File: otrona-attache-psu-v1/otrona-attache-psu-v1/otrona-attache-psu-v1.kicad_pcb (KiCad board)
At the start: 2 copper layers, 258 x 103 mm, 0 parts

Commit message: [otrona] Update schematic, layout, part selection
so far so good... now to print it out and see
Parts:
- added C1: 100uF, Capacitor_THT:CP_Radial_D10.0mm_P5.00mm, F.Cu at (213.9, 44.7)
- added C2: 100uF, Capacitor_THT:CP_Radial_D10.0mm_P5.00mm, F.Cu at (214.1, 26.7)
- added C3: 100uF, Capacitor_THT:CP_Radial_D10.0mm_P5.00mm, F.Cu at (233.2, 84.8)
- added C4: 100uF, Capacitor_THT:CP_Radial_D10.0mm_P5.00mm, F.Cu at (214.1, 14.0)
- added J1: VIDEO, Connector_Phoenix_MSTB:PhoenixContact_MSTBVA_2,5_5-G-5,08_1x05_P5.08mm_Vertical, F.Cu at (250.6, 95.0)
- added J2: CPU, Connector_Phoenix_MSTB:PhoenixContact_MSTBVA_2,5_12-G-5,08_1x12_P5.08mm_Vertical, F.Cu at (232.8, 66.7)
- added J3: DRIVES, Connector_Phoenix_MSTB:PhoenixContact_MSTBVA_2,5_8-G-5,08_1x08_P5.08mm_Vertical, F.Cu at (250.6, 46.1)
- added J4: 15V_CONV, Connector_PinHeader_2.54mm:PinHeader_1x04_P2.54mm_Horizontal, F.Cu at (210.5, 96.6)
- added J5: ATX-24, Connector_Molex:Molex_Mini-Fit_Jr_5566-24A2_2x12_P4.20mm_Vertical, F.Cu at (166.7, 60.9)
- added J6: PWR, Connector_PinHeader_2.54mm:PinHeader_1x02_P2.54mm_Horizontal, F.Cu at (171.5, 94.3)
- added J7: FAN, Connector_PinHeader_2.54mm:PinHeader_1x02_P2.54mm_Horizontal, F.Cu at (162.7, 94.3)
- added L1: 100uH, Inductor_THT:L_Axial_L11.0mm_D4.5mm_P15.24mm_Horizontal_Fastron_MECC, F.Cu at (222.9, 77.4)
- added L2: 100uH, Inductor_THT:L_Axial_L11.0mm_D4.5mm_P15.24mm_Horizontal_Fastron_MECC, F.Cu at (202.3, 34.0)
- added L3: 100uH, Inductor_THT:L_Axial_L11.0mm_D4.5mm_P15.24mm_Horizontal_Fastron_MECC, F.Cu at (202.3, 21.2)
- added L4: 100uH, Inductor_THT:L_Axial_L11.0mm_D4.5mm_P15.24mm_Horizontal_Fastron_MECC, F.Cu at (202.1, 10.1)
- added L5: 100uH, Inductor_THT:L_Axial_L11.0mm_D4.5mm_P15.24mm_Horizontal_Fastron_MECC, F.Cu at (223.0, 60.3)
- added L6: 100uH, Inductor_THT:L_Axial_L11.0mm_D4.5mm_P15.24mm_Horizontal_Fastron_MECC, F.Cu at (186.6, 77.3)

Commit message: [otrona] ok fine i routed the damned board
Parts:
- added J8: AUDIO, Connector_PinHeader_2.54mm:PinHeader_1x02_P2.54mm_Horizontal, F.Cu at (73.0, 109.2)
- moved L2 157.4 mm to (47.6, 63.0), turned to 270 degrees
- moved L3 156.2 mm to (47.6, 42.1), turned to 270 degrees
- moved J3 155.1 mm to (96.6, 64.8)
- moved L4 155.0 mm to (47.6, 21.3), turned to 270 degrees
- moved C3 154.1 mm to (79.4, 95.2)
- moved C2 154.0 mm to (60.8, 41.7)
- moved C4 154.0 mm to (60.8, 29.0)
- moved C1 154.0 mm to (60.6, 59.7)
- moved J2 154.0 mm to (79.5, 81.7)
- moved J4 154.0 mm to (57.2, 111.6)
- moved L1 154.0 mm to (69.7, 92.4)
- moved L5 154.0 mm to (69.7, 75.2)
- moved J1 153.8 mm to (96.8, 98.9)
- moved J5 141.7 mm to (25.3, 70.3)
- moved J7 127.7 mm to (36.2, 111.8)
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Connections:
- J1 pad 5: VIDEO_HSYNC -> DISPLAY_HSYNC
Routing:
- net +5V: track 0.00 -> 141.7 mm, vias 0 -> 1
- net +12V: track 0.00 -> 117.1 mm
- net CPU_12V: track 0.00 -> 101.8 mm
- net CPU_5V: track 0.00 -> 88.9 mm
- net ATX_PSON: track 0.00 -> 73.1 mm
- net ATX_POK: track 0.00 -> 63.3 mm
- net SPK_AUDIO: track 0.00 -> 60.6 mm
- net SPK_GND: track 0.00 -> 48.2 mm
- net CONV_12V: track 0.00 -> 46.1 mm
- net -12V: track 0.00 -> 44.7 mm
- net DISPLAY_VSYNC: track 0.00 -> 39.0 mm
- net DISPLAY_HSYNC: track 0.00 -> 34.5 mm
- net CONV_15V: track 0.00 -> 33.9 mm
- net CPU_MINUS_12V: track 0.00 -> 33.9 mm
- net DISPLAY_15V: track 0.00 -> 32.6 mm
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- added copper zone on B.Cu, net GND
- added copper zone on F.Cu, net GND
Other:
- board size 258 x 103 mm -> 89.8 x 103 mm
- board text added: "+12v"
- board text added: "+5v"
- board text added: "-12v"
- board text added: "100uF"
- board text added: "100uH"
- board text added: "12/15v converter"
- board text added: "12v"
- board text added: "15v"
- board text added: "5v"
- board text added: "<adrian@freebsd.org>"
- board text added: "ATX_ON"
- board text added: "Adrian Chadd"
- board text added: "CPU"
- board text added: "DRIVES"
- board text added: "FAN"
- board text added: "G"
- board text added: "GND"
- board text added: "HS"
- board text added: "HSYNC"
- board text added: "Otrona Attache PSU"
- board text added: "POK"
- board text added: "PSON"
- board text added: "PowerButton"
- board text added: "PwrOk"
- board text added: "SA"
- board text added: "SG"
- board text added: "SPKR"
- board text added: "VIDEO"
- board text added: "VS"
- board text added: "VSYNC"
- board text added: "Video"
- board text added: "v0.1, May 2022"

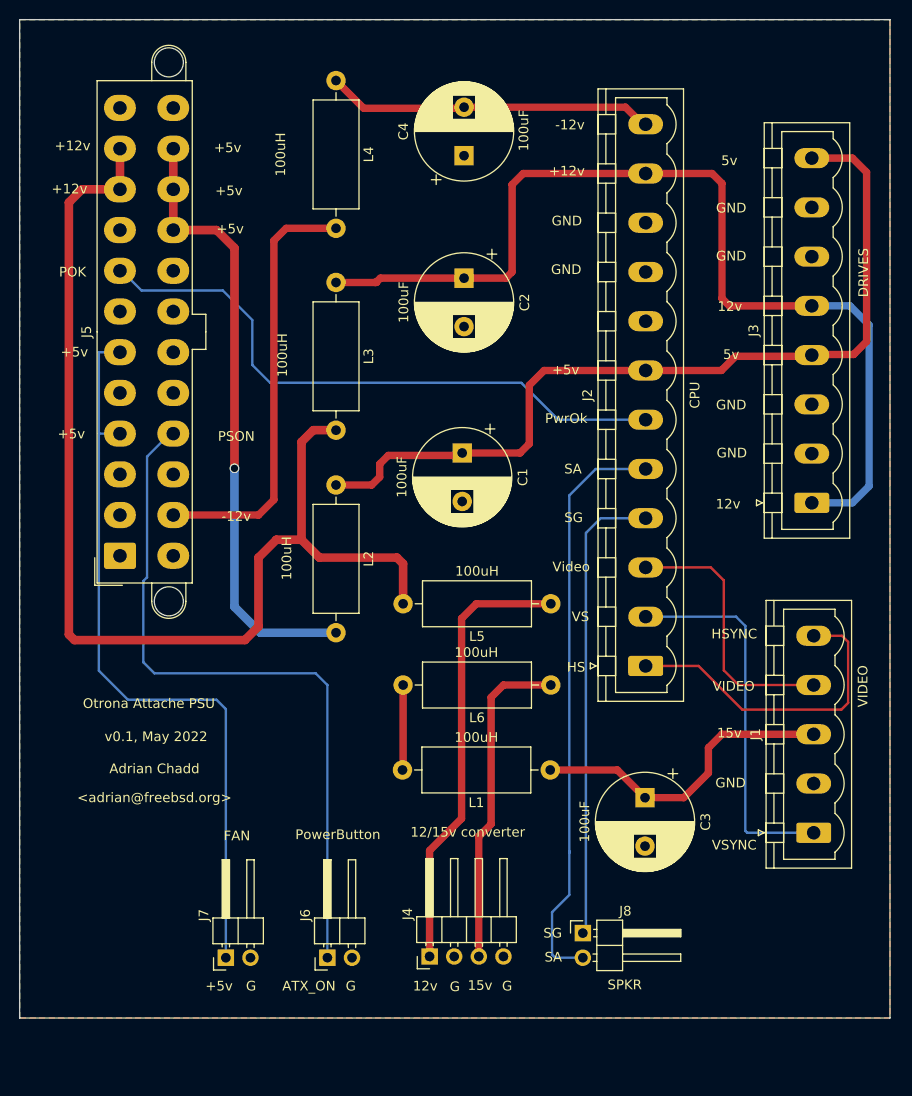
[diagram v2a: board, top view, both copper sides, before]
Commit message: Fix initial hole placings and board size, connector spacing
I still may need to tweak the top/bottom of the board clearance
but at least now this SHOULD work.

Also fix the connector spacing, I got it super bloody wrong.

I still need to fix the pad size on the ATX connector, le sigh.
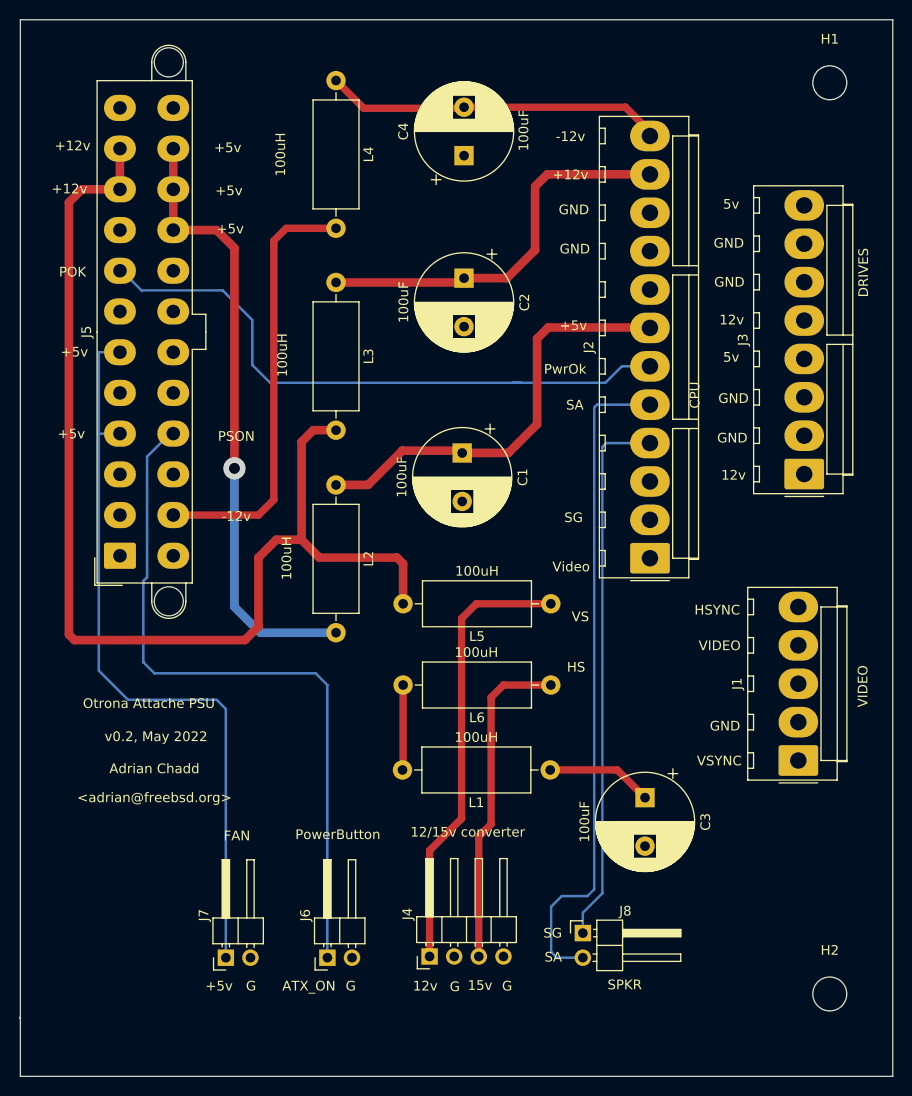
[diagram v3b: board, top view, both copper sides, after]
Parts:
- added H1: MountingHole_Pad, MountingHole:MountingHole_3.5mm, F.Cu at (98.5, 21.5)
- added H2: MountingHole_Pad, MountingHole:MountingHole_3.5mm, F.Cu at (98.5, 115.5)
- J1: footprint Connector_Phoenix_MSTB:PhoenixContact_MSTBVA_2,5_5-G-5,08_1x05_P5.08mm_Vertical -> Connector_Molex:Molex_KK-396_A-41791-0005_1x05_P3.96mm_Vertical
- J2: footprint Connector_Phoenix_MSTB:PhoenixContact_MSTBVA_2,5_12-G-5,08_1x12_P5.08mm_Vertical -> Connector_Molex:Molex_KK-396_A-41791-0012_1x12_P3.96mm_Vertical
- J3: footprint Connector_Phoenix_MSTB:PhoenixContact_MSTBVA_2,5_8-G-5,08_1x08_P5.08mm_Vertical -> Connector_Molex:Molex_KK-396_A-41791-0008_1x08_P3.96mm_Vertical
- moved J2 11.1 mm to (80.0, 70.5)
- moved J1 7.62 mm to (95.3, 91.4)
- moved J3 3.07 mm to (95.9, 61.9)
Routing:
- net CPU_12V: track 101.8 -> 40.8 mm
- net CPU_5V: track 88.9 -> 44.5 mm
- net DISPLAY_VSYNC: track 39.0 -> 0.00 mm
- net DISPLAY_HSYNC: track 34.5 -> 0.00 mm
- net DISPLAY_VIDEO: track 27.8 -> 0.00 mm
- net DISPLAY_15V: track 32.6 -> 11.0 mm
- net SPK_AUDIO: track 60.6 -> 68.9 mm
- net SPK_GND: track 48.2 -> 56.1 mm
- removed copper zone on B.Cu, net GND
- removed copper zone on F.Cu, net GND
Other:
- board size 89.8 x 103 mm -> 90.1 x 109 mm
- board text added: "v0.2, May 2022"
- board text removed: "v0.1, May 2022"

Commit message: Final update before I printed it!
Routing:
- net CPU_12V: track 40.8 -> 94.4 mm
- net CPU_5V: track 44.5 -> 86.6 mm
- net DISPLAY_VSYNC: track 0.00 -> 38.0 mm
- net DISPLAY_VIDEO: track 0.00 -> 36.8 mm
- net DISPLAY_15V: track 11.0 -> 37.4 mm
- net DISPLAY_HSYNC: track 0.00 -> 19.3 mm
- added copper zone on B.Cu, net GND
- added copper zone on F.Cu, net GND
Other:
- board text added: "v0.2, June 2022"
- board text removed: "v0.2, May 2022"

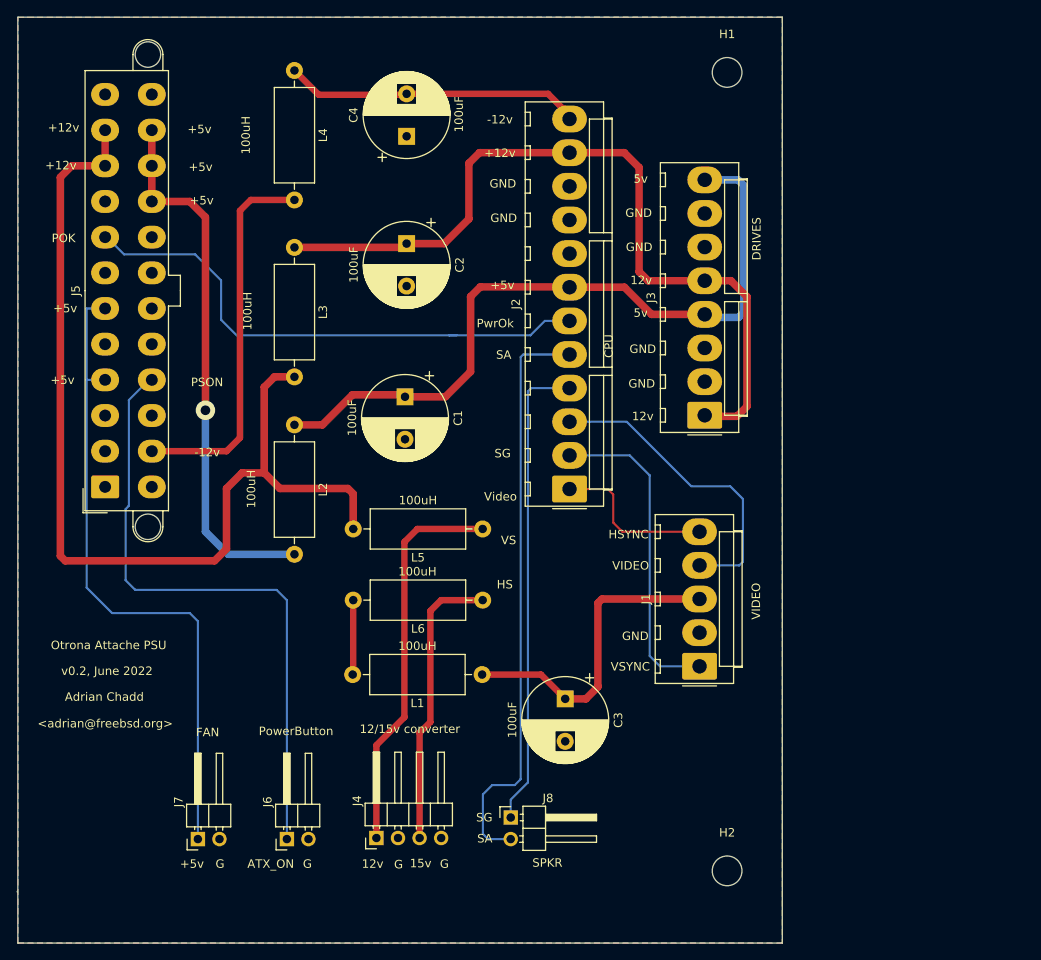
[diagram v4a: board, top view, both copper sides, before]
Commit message: start re-laying things out, after my previous board just didn't fit right.
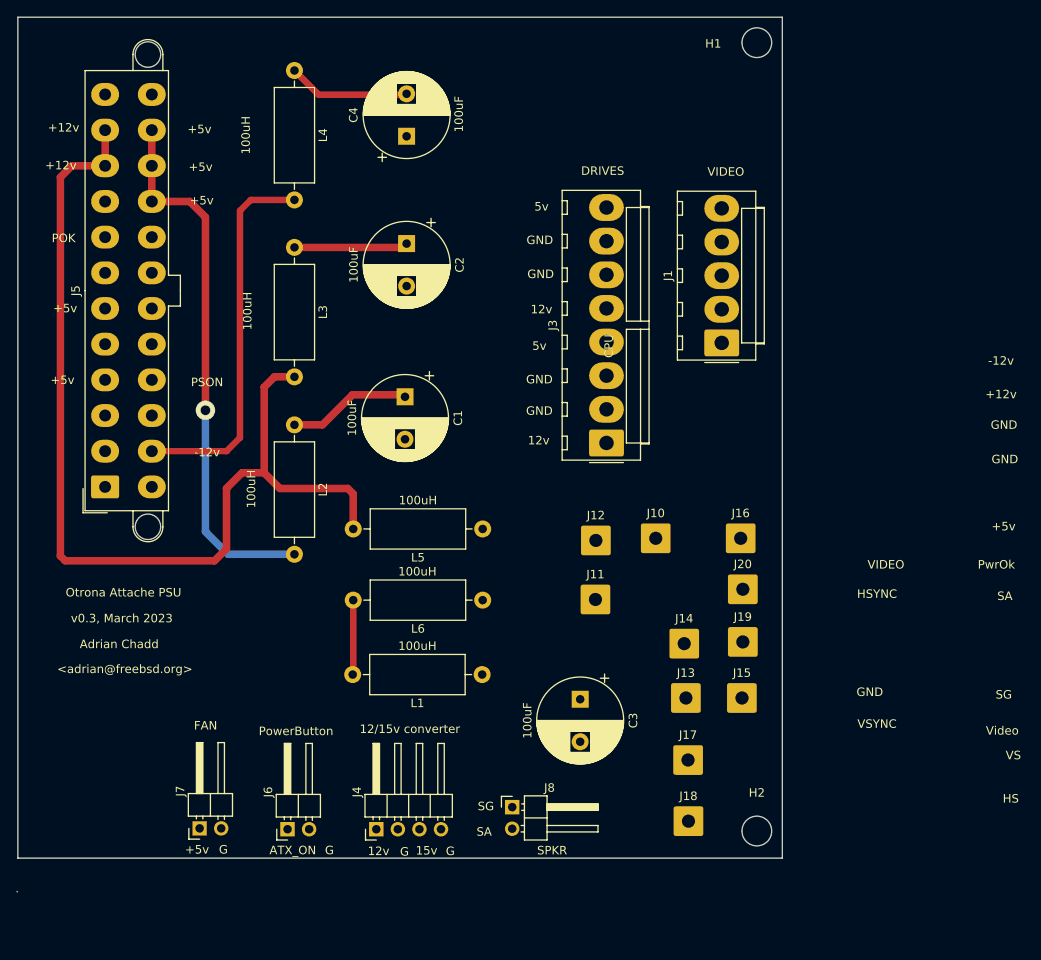
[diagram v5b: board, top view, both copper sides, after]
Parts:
- removed J2: CPU, Connector_Molex:Molex_KK-396_A-41791-0012_1x12_P3.96mm_Vertical
- added J10: HSYNC, Connector_Wire:SolderWire-0.75sqmm_1x01_D1.25mm_OD3.5mm, F.Cu at (90.1, 76.3)
- added J11: VSYNC, Connector_Wire:SolderWire-0.75sqmm_1x01_D1.25mm_OD3.5mm, F.Cu at (83.0, 83.5)
- added J12: VIDEO, Connector_Wire:SolderWire-0.75sqmm_1x01_D1.25mm_OD3.5mm, F.Cu at (83.0, 76.6)
- added J13: SPK_GND, Connector_Wire:SolderWire-0.75sqmm_1x01_D1.25mm_OD3.5mm, F.Cu at (93.7, 95.2)
- added J14: SPK_AUDIO, Connector_Wire:SolderWire-0.75sqmm_1x01_D1.25mm_OD3.5mm, F.Cu at (93.5, 88.8)
- added J15: ATX_POK, Connector_Wire:SolderWire-0.75sqmm_1x01_D1.25mm_OD3.5mm, F.Cu at (100.2, 95.2)
- added J16: 5V, Connector_Wire:SolderWire-0.75sqmm_1x01_D1.25mm_OD3.5mm, F.Cu at (100.1, 76.3)
- added J17: GND, Connector_Wire:SolderWire-0.75sqmm_1x01_D1.25mm_OD3.5mm, F.Cu at (93.9, 102.5)
- added J18: GND, Connector_Wire:SolderWire-0.75sqmm_1x01_D1.25mm_OD3.5mm, F.Cu at (94.0, 109.7)
- added J19: 12V, Connector_Wire:SolderWire-0.75sqmm_1x01_D1.25mm_OD3.5mm, F.Cu at (100.3, 88.5)
- added J20: -12V, Connector_Wire:SolderWire-0.75sqmm_1x01_D1.25mm_OD3.5mm, F.Cu at (100.3, 82.3)
- moved J1 38.2 mm to (97.9, 53.3)
- moved J3 12.0 mm to (84.3, 65.1)
- moved H2 5.85 mm to (102.0, 110.8)
- moved H1 4.95 mm to (102.0, 18.0)
- moved C3 1.76 mm to (81.2, 95.3)
- moved J7 1.28 mm to (36.4, 110.5)
- moved J8 1.23 mm to (73.2, 108.0)
- moved J6 1.16 mm to (46.8, 110.6)
- moved J4 1.03 mm to (57.2, 110.6)
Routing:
- net CPU_12V: track 94.4 -> 13.4 mm
- net +5V: track 141.7 -> 64.1 mm
- net ATX_PSON: track 73.1 -> 0.00 mm
- net CPU_5V: track 86.6 -> 14.6 mm
- net SPK_AUDIO: track 68.9 -> 0.00 mm
- net ATX_POK: track 63.8 -> 0.00 mm
- net SPK_GND: track 56.1 -> 0.00 mm
- net CONV_12V: track 46.1 -> 0.00 mm
- net DISPLAY_VSYNC: track 38.0 -> 0.00 mm
- net DISPLAY_15V: track 37.4 -> 0.00 mm
- net DISPLAY_VIDEO: track 36.8 -> 0.00 mm
- net CONV_15V: track 33.9 -> 0.00 mm
- net CPU_MINUS_12V: track 33.9 -> 14.4 mm
- net DISPLAY_HSYNC: track 19.3 -> 0.00 mm
- removed copper zone on B.Cu, net GND
- removed copper zone on F.Cu, net GND
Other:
- board size 90.1 x 109 mm -> 90.1 x 103 mm
- board text added: "v0.3, March 2023"
- board text removed: "v0.2, June 2022"

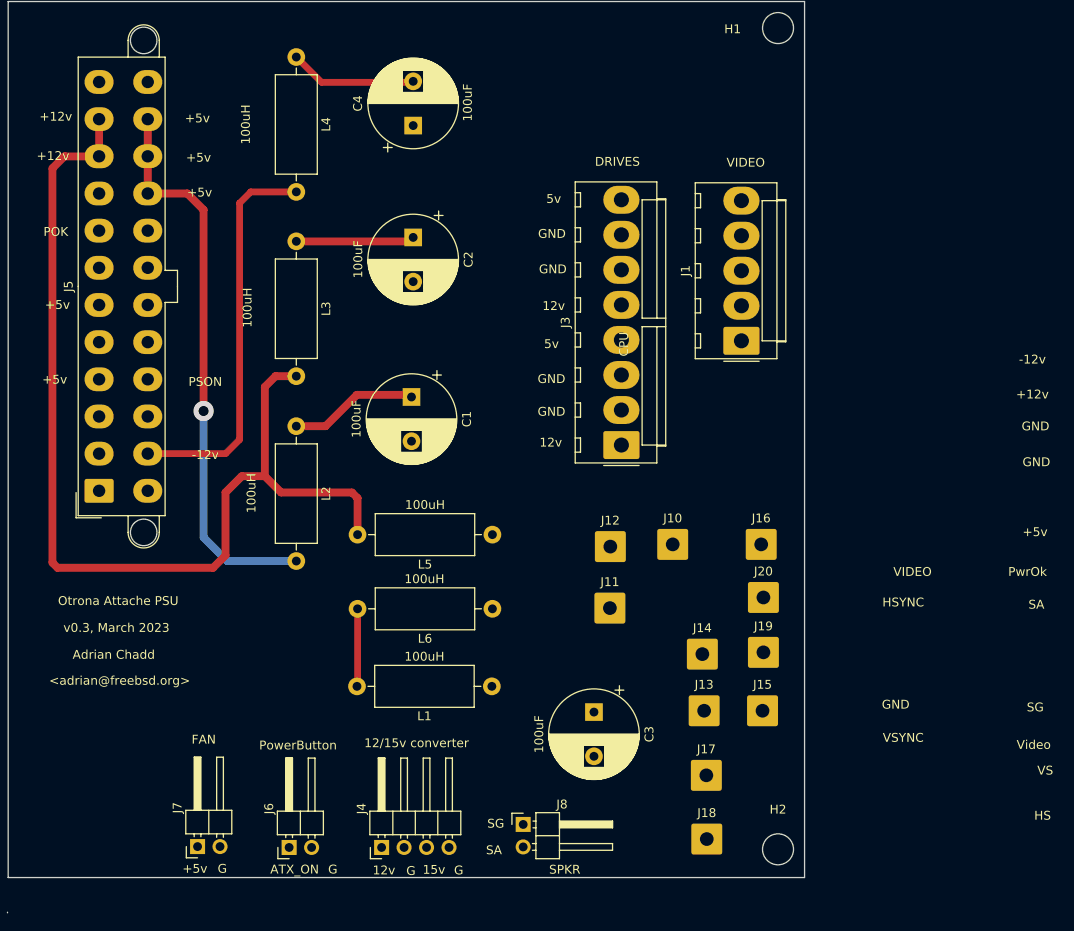
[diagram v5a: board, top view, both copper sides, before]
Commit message: more layout changes
i haven't put in the ground planes yet, but now all of the CPU board wiring is
hopefully in the right place for it to reach.
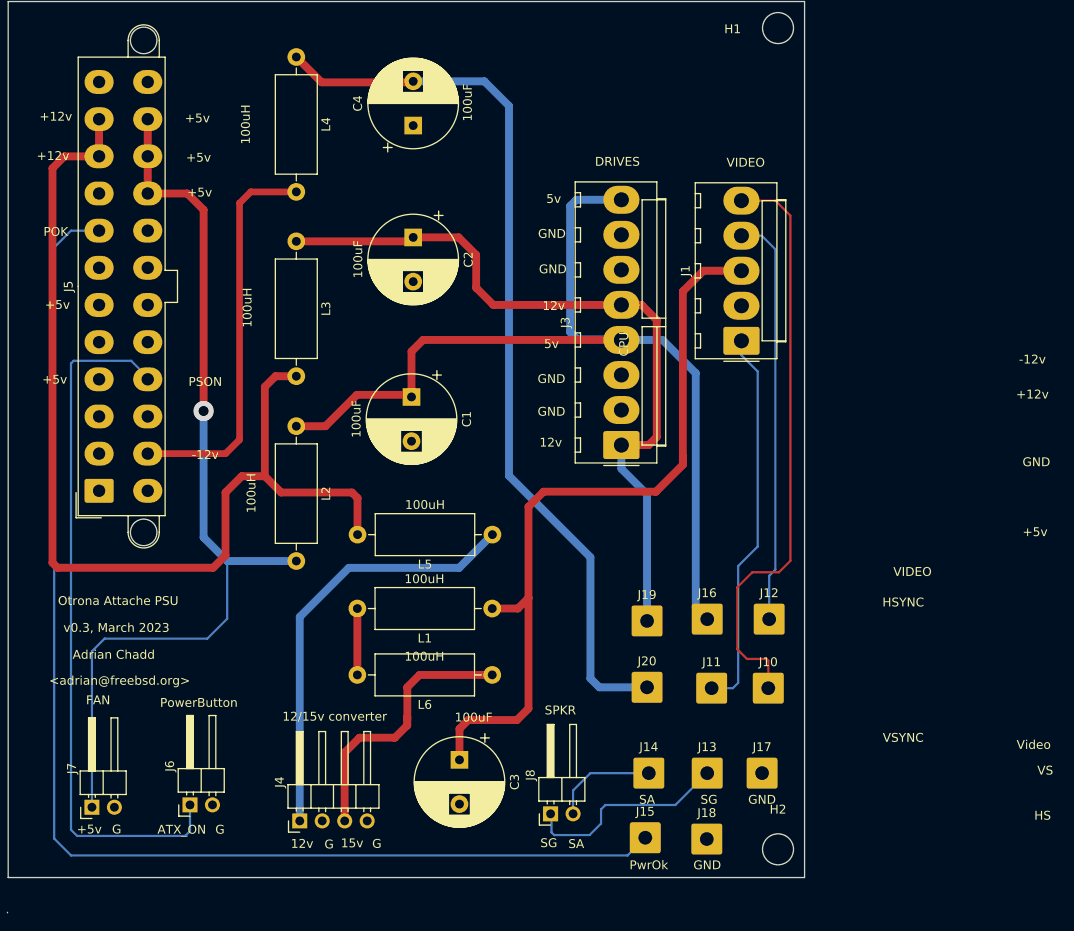
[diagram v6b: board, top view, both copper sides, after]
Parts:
- moved J12 19.7 mm to (101.0, 84.8)
- moved J15 19.5 mm to (87.0, 109.5)
- moved J10 19.5 mm to (100.9, 92.6)
- moved J20 16.6 mm to (87.2, 92.5)
- moved C3 16.1 mm to (66.0, 100.7)
- moved J14 14.7 mm to (87.4, 102.2)
- moved J11 14.6 mm to (94.5, 92.6)
- moved J19 13.6 mm to (87.2, 85.0)
- moved J7 12.7 mm to (24.5, 106.1)
- moved J6 12.2 mm to (35.5, 105.8)
- moved J16 10.4 mm to (94.0, 84.8)
- moved J4 9.72 mm to (48.0, 107.6)
- moved L1 8.79 mm to (69.7, 83.6)
- moved L6 7.47 mm to (69.7, 91.1)
- moved J13 7.06 mm to (94.0, 102.2)
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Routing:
- net ATX_POK: track 0.00 -> 141.1 mm
- net CPU_5V: track 14.6 -> 108.8 mm
- net CPU_MINUS_12V: track 14.4 -> 101.7 mm
- net DISPLAY_15V: track 0.00 -> 87.0 mm
- net ATX_PSON: track 0.00 -> 79.4 mm
- net CPU_12V: track 13.4 -> 85.6 mm
- net DISPLAY_HSYNC: track 0.00 -> 66.6 mm
- net CONV_12V: track 0.00 -> 48.7 mm
- net DISPLAY_VIDEO: track 0.00 -> 46.6 mm
- net DISPLAY_VSYNC: track 0.00 -> 43.6 mm
- net +5V: track 64.1 -> 105.0 mm
- net CONV_15V: track 0.00 -> 30.9 mm
- net SPK_GND: track 0.00 -> 23.7 mm
- net SPK_AUDIO: track 0.00 -> 12.0 mm
- net +15V: track 8.79 -> 7.50 mm
